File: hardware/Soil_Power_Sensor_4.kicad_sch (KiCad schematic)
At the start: 15 parts, among them J6 UART, SW1 EN, SW2 BOOT, U9 ESP32-C3-WROOM-02-N4

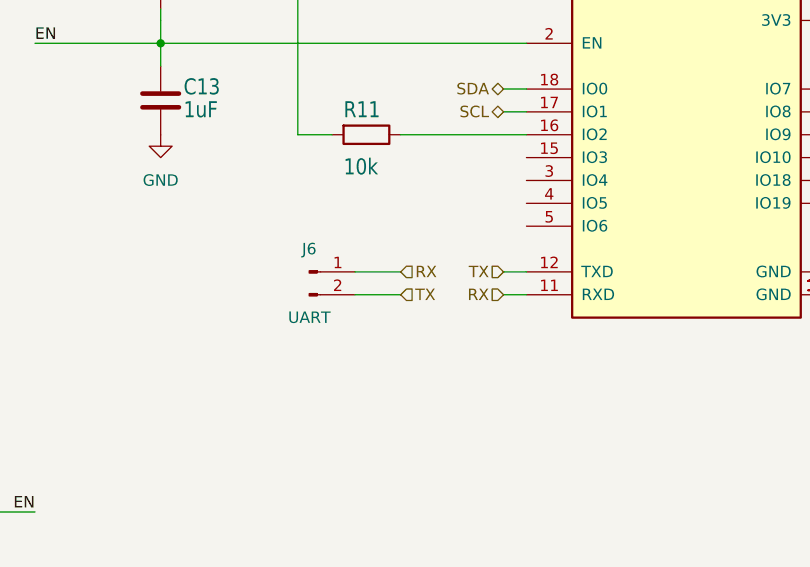
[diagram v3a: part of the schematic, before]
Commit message: Fixed ERC errors
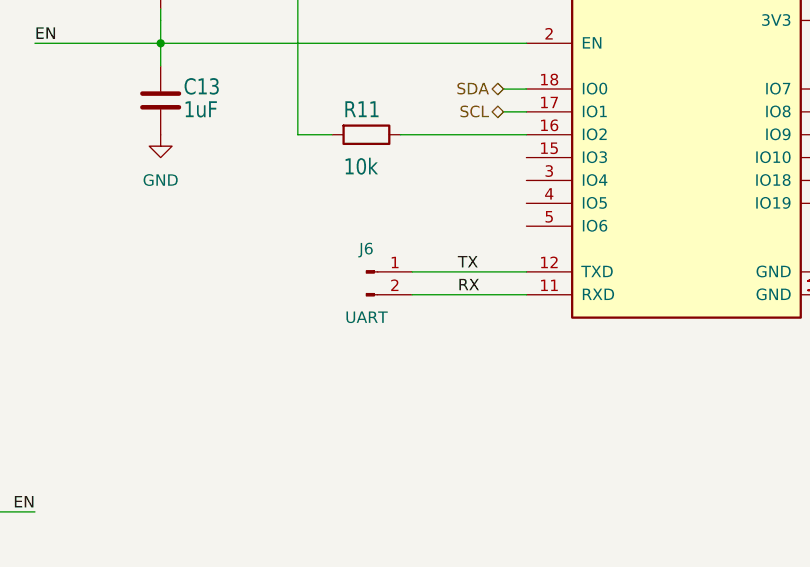
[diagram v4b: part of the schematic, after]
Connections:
- net RX: now also J6.2 (Pin_2); no longer J6.1 (Pin_1)
- net TX: now also J6.1 (Pin_1); no longer J6.2 (Pin_2)
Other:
- moved on the sheet: J6
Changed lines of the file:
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@@
     (stroke (width 0) (type default))
   )
-  (wire (pts (xy 144.78 104.14) (xy 147.32 104.14))
+  (wire (pts (xy 134.62 104.14) (xy 147.32 104.14))
     (stroke (width 0) (type default))
   )
@@
     (stroke (width 0.1524) (type solid))
   )
-  (wire (pts (xy 128.27 104.14) (xy 133.35 104.14))
-    (stroke (width 0) (type default))
-  )
   (wire (pts (xy 147.32 86.36) (xy 144.78 86.36))
     (stroke (width 0.1524) (type solid))
   )
-  (wire (pts (xy 144.78 106.68) (xy 147.32 106.68))
-    (stroke (width 0) (type default))
-  )
   (wire (pts (xy 48.26 137.16) (xy 57.15 137.16))
     (stroke (width 0) (type default))
@@
     (stroke (width 0.1524) (type solid))
   )
-  (wire (pts (xy 128.27 106.68) (xy 133.35 106.68))
+  (wire (pts (xy 134.62 106.68) (xy 147.32 106.68))
     (stroke (width 0) (type default))
   )
@@
     (effects (font (size 1.27 1.27)) (justify right bottom))
   )
+  (label "TX" (at 139.7 104.14 0) (fields_autoplaced)
+    (effects (font (size 1.27 1.27)) (justify left bottom))
+  )
   (label "EN" (at 92.71 78.74 0) (fields_autoplaced)
     (effects (font (size 1.27 1.27)) (justify left bottom))
   )
+  (label "RX" (at 139.7 106.68 0) (fields_autoplaced)
+    (effects (font (size 1.27 1.27)) (justify left bottom))
+  )
   (label "BOOT" (at 193.04 88.9 180) (fields_autoplaced)
     (effects (font (size 1.27 1.27)) (justify right bottom))
@@
   (hierarchical_label "SDA" (shape bidirectional) (at 144.78 83.82 180) (fields_autoplaced)
     (effects (font (size 1.27 1.27)) (justify right))
-  )
-  (hierarchical_label "RX" (shape input) (at 133.35 104.14 0) (fields_autoplaced)
-    (effects (font (size 1.27 1.27)) (justify left))
-  )
-  (hierarchical_label "TX" (shape input) (at 144.78 104.14 180) (fields_autoplaced)
-    (effects (font (size 1.27 1.27)) (justify right))
-  )
-  (hierarchical_label "RX" (shape input) (at 144.78 106.68 180) (fields_autoplaced)
-    (effects (font (size 1.27 1.27)) (justify right))
-  )
-  (hierarchical_label "TX" (shape input) (at 133.35 106.68 0) (fields_autoplaced)
-    (effects (font (size 1.27 1.27)) (justify left))
   )
   (hierarchical_label "ESP32_EN" (shape input) (at 88.9 63.5 180) (fields_autoplaced)
@@
     )
   )
-  (symbol (lib_id "Connector:Conn_01x02_Pin") (at 123.19 104.14 0) (unit 1)
-    (in_bom yes) (on_board yes) (dnp no)
-    (property "Reference" "J6" (at 123.19 101.6 0)
-      (effects (font (size 1.27 1.27)))
-    )
-    (property "Value" "UART" (at 123.19 109.22 0)
-      (effects (font (size 1.27 1.27)))
-    )
-    (property "Footprint" "Connector_PinHeader_2.54mm:PinHeader_1x02_P2.54mm_Vertical" (at 123.19 104.14 0)
-      (effects (font (size 1.27 1.27)) hide)
-    )
-    (property "Datasheet" "~" (at 123.19 104.14 0)
-      (effects (font (size 1.27 1.27)) hide)
-    )
+  (symbol (lib_id "Connector:Conn_01x02_Pin") (at 129.54 104.14 0) (unit 1)
+    (in_bom yes) (on_board yes) (dnp no)
+    (property "Reference" "J6" (at 129.54 101.6 0)
+      (effects (font (size 1.27 1.27)))
+    )
+    (property "Value" "UART" (at 129.54 109.22 0)
+      (effects (font (size 1.27 1.27)))
+    )
+    (property "Footprint" "Connector_PinHeader_2.54mm:PinHeader_1x02_P2.54mm_Vertical" (at 129.54 104.14 0)
+      (effects (font (size 1.27 1.27)) hide)
+    )
+    (property "Datasheet" "~" (at 129.54 104.14 0)
+      (effects (font (size 1.27 1.27)) hide)
+    )

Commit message: Updated board layout
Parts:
- removed JP5: ESP_EN, symbol Jumper:SolderJumper_2_Open
- removed JP6: ESP_EN_3V3, symbol Jumper:SolderJumper_2_Bridged
- added JP5: ESP_EN, Jumper:SolderJumper-3_P1.3mm_Open_Pad1.0x1.5mm, symbol Jumper:SolderJumper_3_Bridged12
- JP4: footprint (none) -> Jumper:SolderJumper-2_P1.3mm_Open_Pad1.0x1.5mm
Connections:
- net +3V3: now also JP5.1 (A)
- net ESP32_EN: now also JP5.3 (B)
- net at R12.1: now also JP5.2 (C)
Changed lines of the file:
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@@
   (junction (at 187.96 106.68) (diameter 0) (color 0 0 0 0)
   )
-  (junction (at 106.68 63.5) (diameter 0) (color 0 0 0 0)
-  )
   (junction (at 210.82 68.58) (diameter 0) (color 0 0 0 0)
   )
   (junction (at 106.68 78.74) (diameter 0) (color 0 0 0 0)
   )
-  (wire (pts (xy 106.68 63.5) (xy 106.68 67.31))
-    (stroke (width 0) (type default))
-  )
   (wire (pts (xy 121.92 88.9) (xy 121.92 71.12))
     (stroke (width 0.1524) (type solid))
   )
-  (wire (pts (xy 106.68 52.07) (xy 106.68 53.34))
+  (wire (pts (xy 114.3 58.42) (xy 114.3 63.5))
     (stroke (width 0) (type default))
   )
@@
     (stroke (width 0) (type default))
   )
-  (wire (pts (xy 100.33 63.5) (xy 106.68 63.5))
-    (stroke (width 0.1524) (type solid))
-  )
   (wire (pts (xy 64.77 137.16) (xy 72.39 137.16))
     (stroke (width 0) (type default))
   )
-  (wire (pts (xy 88.9 63.5) (xy 92.71 63.5))
-    (stroke (width 0) (type default))
-  )
   (wire (pts (xy 220.98 68.58) (xy 210.82 68.58))
     (stroke (width 0.1524) (type solid))
@@
     (stroke (width 0) (type default))
   )
+  (wire (pts (xy 92.71 63.5) (xy 101.6 63.5))
+    (stroke (width 0) (type default))
+  )
   (wire (pts (xy 106.68 76.2) (xy 106.68 78.74))
     (stroke (width 0.1524) (type solid))
@@
     (stroke (width 0.1524) (type solid))
   )
+  (wire (pts (xy 114.3 63.5) (xy 111.76 63.5))
+    (stroke (width 0) (type default))
+  )
   (wire (pts (xy 210.82 76.2) (xy 210.82 68.58))
     (stroke (width 0.1524) (type solid))
@@
   )
   (wire (pts (xy 48.26 130.81) (xy 55.88 130.81))
-    (stroke (width 0) (type default))
-  )
-  (wire (pts (xy 106.68 60.96) (xy 106.68 63.5))
     (stroke (width 0) (type default))
   )
@@
     (effects (font (size 1.27 1.27)) (justify right))
   )
-  (hierarchical_label "ESP32_EN" (shape input) (at 88.9 63.5 180) (fields_autoplaced)
+  (hierarchical_label "ESP32_EN" (shape input) (at 92.71 63.5 180) (fields_autoplaced)
     (effects (font (size 1.27 1.27)) (justify right))
   )
@@
         (path "/5300ec4d-4648-40a1-8d89-4fa6b3bf32a3/1383843a-880b-4efd-8c7f-ecdf3639f794"
           (reference "C16") (unit 1)
-        )
-      )
-    )
-  )
-  (symbol (lib_id "Jumper:SolderJumper_2_Bridged") (at 106.68 57.15 270) (unit 1)
-    (in_bom yes) (on_board yes) (dnp no) (fields_autoplaced)
-    (property "Reference" "JP6" (at 109.22 55.88 90)
-      (effects (font (size 1.27 1.27)) (justify left))
-    )
-    (property "Value" "ESP_EN_3V3" (at 109.22 58.42 90)
-      (effects (font (size 1.27 1.27)) (justify left))
-    )
-    (property "Footprint" "" (at 106.68 57.15 0)
-      (effects (font (size 1.27 1.27)) hide)
-    )
-    (property "Datasheet" "~" (at 106.68 57.15 0)
-      (effects (font (size 1.27 1.27)) hide)
-    )
-    (pin "1")
-    (pin "2")
-    (instances
-      (project "Soil Power Sensor"
-        (path "/5300ec4d-4648-40a1-8d89-4fa6b3bf32a3/1383843a-880b-4efd-8c7f-ecdf3639f794"
-          (reference "JP6") (unit 1)
         )
       )
@@
     )
   )
-  (symbol (lib_id "Jumper:SolderJumper_2_Open") (at 96.52 63.5 0) (unit 1)
-    (in_bom yes) (on_board yes) (dnp no) (fields_autoplaced)
-    (property "Reference" "JP5" (at 96.52 57.15 0)
-      (effects (font (size 1.27 1.27)))
-    )
-    (property "Value" "ESP_EN" (at 96.52 59.69 0)
-      (effects (font (size 1.27 1.27)))
-    )
-    (property "Footprint" "" (at 96.52 63.5 0)
-      (effects (font (size 1.27 1.27)) hide)
-    )
-    (property "Datasheet" "~" (at 96.52 63.5 0)
-      (effects (font (size 1.27 1.27)) hide)
-    )
-    (pin "2")
-    (pin "1")
-    (instances
-      (project "Soil Power Sensor"
-        (path "/5300ec4d-4648-40a1-8d89-4fa6b3bf32a3/1383843a-880b-4efd-8c7f-ecdf3639f794"
-          (reference "JP5") (unit 1)
-        )
-      )
-    )
-  )
   (symbol (lib_id "power:+3V3") (at 121.92 71.12 0) (unit 1)
     (in_bom yes) (on_board yes) (dnp no)
@@
       (effects (font (size 1.27 1.27)))
     )
-    (property "Footprint" "" (at 81.28 130.81 0)
+    (property "Footprint" "Jumper:SolderJumper-2_P1.3mm_Open_Pad1.0x1.5mm" (at 81.28 130.81 0)
       (effects (font (size 1.27 1.27)) hide)
     )
@@
     )
   )
-  (symbol (lib_id "power:+3V3") (at 106.68 52.07 0) (unit 1)
-    (in_bom yes) (on_board yes) (dnp no)
-    (property "Reference" "#+3V09" (at 106.68 52.07 0)
-      (effects (font (size 1.27 1.27)) hide)
-    )
-    (property "Value" "+3V3" (at 102.87 46.99 0)
-      (effects (font (size 1.778 1.5113)) (justify left top))
-    )
-    (property "Footprint" "" (at 106.68 52.07 0)
-      (effects (font (size 1.27 1.27)) hide)
-    )
-    (property "Datasheet" "" (at 106.68 52.07 0)
+  (symbol (lib_id "power:+3V3") (at 114.3 58.42 0) (unit 1)
+    (in_bom yes) (on_board yes) (dnp no)
+    (property "Reference" "#+3V09" (at 114.3 58.42 0)
+      (effects (font (size 1.27 1.27)) hide)
+    )
+    (property "Value" "+3V3" (at 110.49 53.34 0)
+      (effects (font (size 1.778 1.5113)) (justify left top))
+    )
+    (property "Footprint" "" (at 114.3 58.42 0)
+      (effects (font (size 1.27 1.27)) hide)
+    )
+    (property "Datasheet" "" (at 114.3 58.42 0)
       (effects (font (size 1.27 1.27)) hide)
     )
@@
         )
       )
+    )
+  )
+  (symbol (lib_id "Jumper:SolderJumper_3_Bridged12") (at 106.68 63.5 0) (mirror y) (unit 1)
+    (in_bom yes) (on_board yes) (dnp no)
+    (property "Reference" "JP5" (at 106.68 57.15 0)
+      (effects (font (size 1.27 1.27)))
+    )
+    (property "Value" "ESP_EN" (at 106.68 59.69 0)
+      (effects (font (size 1.27 1.27)))
+    )
+    (property "Footprint" "Jumper:SolderJumper-3_P1.3mm_Open_Pad1.0x1.5mm" (at 106.68 63.5 0)
+      (effects (font (size 1.27 1.27)) hide)
+    )
+    (property "Datasheet" "~" (at 106.68 63.5 0)
+      (effects (font (size 1.27 1.27)) hide)
+    )
+    (pin "2")
+    (pin "3")
+    (pin "1")
+    (instances
+      (project "Soil Power Sensor"
+        (path "/5300ec4d-4648-40a1-8d89-4fa6b3bf32a3/1383843a-880b-4efd-8c7f-ecdf3639f794"
+          (reference "JP5") (unit 1)
+        )
+      )
